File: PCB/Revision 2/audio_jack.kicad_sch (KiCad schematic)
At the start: 1 part, among them J3 AudioJack

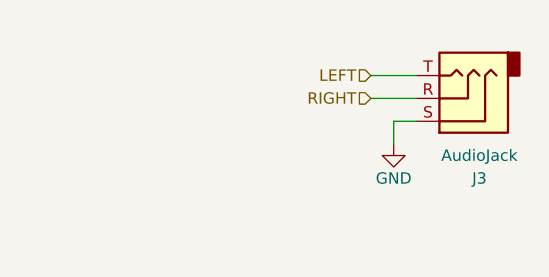
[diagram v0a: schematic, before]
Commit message: ESD protection diodes go BRRRRRRR
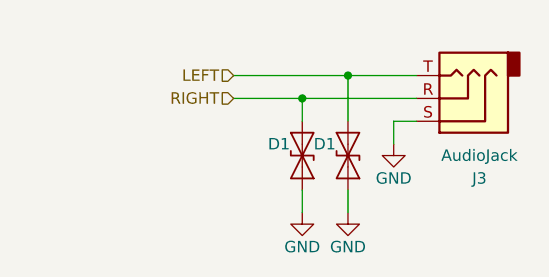
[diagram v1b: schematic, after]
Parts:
- added D1 (x2): ESD9B3.3ST5G, Diode_SMD:D_SOD-923, symbol Diode:ESD9B3.3ST5G
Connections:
- net GND: now also D1.2 (A2), D1.2 (A2)
- net LEFT: now also D1.1 (A1)
- net RIGHT: now also D1.1 (A1)
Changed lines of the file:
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@@
 (kicad_sch (version 20230121) (generator eeschema)
   (paper "USLetter")
+  (junction (at 130.81 86.36) (diameter 0) (color 0 0 0 0)
+  )
+  (junction (at 125.73 88.9) (diameter 0) (color 0 0 0 0)
+  )
+  (wire (pts (xy 130.81 86.36) (xy 138.43 86.36))
+    (stroke (width 0) (type default))
+  )
   (wire (pts (xy 135.89 91.44) (xy 138.43 91.44))
     (stroke (width 0) (type default))
   )
+  (wire (pts (xy 125.73 99.06) (xy 125.73 101.6))
+    (stroke (width 0) (type default))
+  )
   (wire (pts (xy 135.89 91.44) (xy 135.89 93.98))
     (stroke (width 0) (type default))
   )
-  (wire (pts (xy 133.35 88.9) (xy 138.43 88.9))
-    (stroke (width 0) (type default))
-  )
-  (wire (pts (xy 133.35 86.36) (xy 138.43 86.36))
-    (stroke (width 0) (type default))
-  )
-  (hierarchical_label "LEFT" (shape input) (at 133.35 86.36 180) (fields_autoplaced)
+  (wire (pts (xy 130.81 99.06) (xy 130.81 101.6))
+    (stroke (width 0) (type default))
+  )
+  (wire (pts (xy 118.11 88.9) (xy 125.73 88.9))
+    (stroke (width 0) (type default))
+  )
+  (wire (pts (xy 125.73 88.9) (xy 138.43 88.9))
+    (stroke (width 0) (type default))
+  )
+  (wire (pts (xy 118.11 86.36) (xy 130.81 86.36))
+    (stroke (width 0) (type default))
+  )
+  (wire (pts (xy 130.81 86.36) (xy 130.81 91.44))
+    (stroke (width 0) (type default))
+  )
+  (wire (pts (xy 125.73 88.9) (xy 125.73 91.44))
+    (stroke (width 0) (type default))
+  )
+  (hierarchical_label "LEFT" (shape input) (at 118.11 86.36 180) (fields_autoplaced)
     (effects (font (size 1.27 1.27)) (justify right))
   )
-  (hierarchical_label "RIGHT" (shape input) (at 133.35 88.9 180) (fields_autoplaced)
+  (hierarchical_label "RIGHT" (shape input) (at 118.11 88.9 180) (fields_autoplaced)
     (effects (font (size 1.27 1.27)) (justify right))
   )
@@
         (path "/3ba39048-ccb5-49b6-bc29-f9a8dd2e53b6/6aabb2d5-86ec-4e4f-b3fd-74d490a8ab06"
           (reference "#PWR0132") (unit 1)
+        )
+      )
+    )
+  )
+  (symbol (lib_id "Diode:ESD9B3.3ST5G") (at 125.73 95.25 270) (unit 1)
+    (in_bom yes) (on_board yes) (dnp no)
+    (property "Reference" "D1" (at 121.92 93.9799 90)
+      (effects (font (size 1.27 1.27)) (justify left))
+    )
+    (property "Value" "ESD9B3.3ST5G" (at 128.27 96.5199 90)
+      (effects (font (size 1.27 1.27)) (justify left) hide)
+    )
+    (property "Footprint" "Diode_SMD:D_SOD-923" (at 125.73 95.25 0)
+      (effects (font (size 1.27 1.27)) hide)
+    )
+    (property "Datasheet" "https://www.onsemi.com/pub/Collateral/ESD9B-D.PDF" (at 125.73 95.25 0)
+      (effects (font (size 1.27 1.27)) hide)
+    )
+    (pin "1")
+    (pin "2")
+    (instances
+      (project "Revision 2"
+        (path "/3ba39048-ccb5-49b6-bc29-f9a8dd2e53b6/e0049583-c97a-4b82-a4d7-59c894eac2f8"
+          (reference "D1") (unit 1)
+        )
+        (path "/3ba39048-ccb5-49b6-bc29-f9a8dd2e53b6/ef7f0437-b22e-4c24-9273-d90d53267996"
+          (reference "D1") (unit 1)
+        )
+        (path "/3ba39048-ccb5-49b6-bc29-f9a8dd2e53b6/05c17752-4e2f-4780-999c-64683914a9ff"
+          (reference "D18") (unit 1)
+        )
+        (path "/3ba39048-ccb5-49b6-bc29-f9a8dd2e53b6/c07b2ed0-3ddf-4a7b-83a6-b9bc424f9605"
+          (reference "D27") (unit 1)
+        )
+        (path "/3ba39048-ccb5-49b6-bc29-f9a8dd2e53b6/6aabb2d5-86ec-4e4f-b3fd-74d490a8ab06"
+          (reference "D41") (unit 1)
+        )
+      )
+    )
+  )
+  (symbol (lib_id "power:GND") (at 125.73 101.6 0) (unit 1)
+    (in_bom yes) (on_board yes) (dnp no)
+    (property "Reference" "#PWR031" (at 125.73 107.95 0)
+      (effects (font (size 1.27 1.27)) hide)
+    )
+    (property "Value" "GND" (at 125.73 105.41 0)
+      (effects (font (size 1.27 1.27)))
+    )
+    (property "Footprint" "" (at 125.73 101.6 0)
+      (effects (font (size 1.27 1.27)) hide)
+    )
+    (property "Datasheet" "" (at 125.73 101.6 0)
+      (effects (font (size 1.27 1.27)) hide)
+    )
+    (pin "1")
+    (instances
+      (project "Revision 2"
+        (path "/3ba39048-ccb5-49b6-bc29-f9a8dd2e53b6"
+          (reference "#PWR031") (unit 1)
+        )
+        (path "/3ba39048-ccb5-49b6-bc29-f9a8dd2e53b6/ef7f0437-b22e-4c24-9273-d90d53267996"
+          (reference "#PWR0154") (unit 1)
+        )
+        (path "/3ba39048-ccb5-49b6-bc29-f9a8dd2e53b6/05c17752-4e2f-4780-999c-64683914a9ff"
+          (reference "#PWR0168") (unit 1)
+        )
+        (path "/3ba39048-ccb5-49b6-bc29-f9a8dd2e53b6/c07b2ed0-3ddf-4a7b-83a6-b9bc424f9605"
+          (reference "#PWR0177") (unit 1)
+        )
+        (path "/3ba39048-ccb5-49b6-bc29-f9a8dd2e53b6/6aabb2d5-86ec-4e4f-b3fd-74d490a8ab06"
+          (reference "#PWR0191") (unit 1)
+        )
+      )
+    )
+  )
+  (symbol (lib_id "power:GND") (at 130.81 101.6 0) (unit 1)
+    (in_bom yes) (on_board yes) (dnp no)
+    (property "Reference" "#PWR031" (at 130.81 107.95 0)
+      (effects (font (size 1.27 1.27)) hide)
+    )
+    (property "Value" "GND" (at 130.81 105.41 0)
+      (effects (font (size 1.27 1.27)))
+    )
+    (property "Footprint" "" (at 130.81 101.6 0)
+      (effects (font (size 1.27 1.27)) hide)
+    )
+    (property "Datasheet" "" (at 130.81 101.6 0)
+      (effects (font (size 1.27 1.27)) hide)
+    )
+    (pin "1")
+    (instances
+      (project "Revision 2"
+        (path "/3ba39048-ccb5-49b6-bc29-f9a8dd2e53b6"
+          (reference "#PWR031") (unit 1)
+        )
+        (path "/3ba39048-ccb5-49b6-bc29-f9a8dd2e53b6/ef7f0437-b22e-4c24-9273-d90d53267996"
+          (reference "#PWR0154") (unit 1)
+        )
+        (path "/3ba39048-ccb5-49b6-bc29-f9a8dd2e53b6/05c17752-4e2f-4780-999c-64683914a9ff"
+          (reference "#PWR0168") (unit 1)
+        )
+        (path "/3ba39048-ccb5-49b6-bc29-f9a8dd2e53b6/c07b2ed0-3ddf-4a7b-83a6-b9bc424f9605"
+          (reference "#PWR0177") (unit 1)
+        )
+        (path "/3ba39048-ccb5-49b6-bc29-f9a8dd2e53b6/6aabb2d5-86ec-4e4f-b3fd-74d490a8ab06"
+          (reference "#PWR0190") (unit 1)
         )
       )
@@
         )
       )
+    )
+  )
+  (symbol (lib_id "Diode:ESD9B3.3ST5G") (at 130.81 95.25 270) (unit 1)
+    (in_bom yes) (on_board yes) (dnp no)
+    (property "Reference" "D1" (at 127 93.9799 90)
+      (effects (font (size 1.27 1.27)) (justify left))
+    )
+    (property "Value" "ESD9B3.3ST5G" (at 133.35 96.5199 90)
+      (effects (font (size 1.27 1.27)) (justify left) hide)
+    )
+    (property "Footprint" "Diode_SMD:D_SOD-923" (at 130.81 95.25 0)
+      (effects (font (size 1.27 1.27)) hide)
+    )
+    (property "Datasheet" "https://www.onsemi.com/pub/Collateral/ESD9B-D.PDF" (at 130.81 95.25 0)
+      (effects (font (size 1.27 1.27)) hide)
+    )
+    (pin "1")
+    (pin "2")
+    (instances
+      (project "Revision 2"
+        (path "/3ba39048-ccb5-49b6-bc29-f9a8dd2e53b6/e0049583-c97a-4b82-a4d7-59c894eac2f8"
+          (reference "D1") (unit 1)
+        )
+        (path "/3ba39048-ccb5-49b6-bc29-f9a8dd2e53b6/ef7f0437-b22e-4c24-9273-d90d53267996"
+          (reference "D1") (unit 1)
+        )
+        (path "/3ba39048-ccb5-49b6-bc29-f9a8dd2e53b6/05c17752-4e2f-4780-999c-64683914a9ff"
+          (reference "D18") (unit 1)
+        )
+        (path "/3ba39048-ccb5-49b6-bc29-f9a8dd2e53b6/c07b2ed0-3ddf-4a7b-83a6-b9bc424f9605"
+          (reference "D27") (unit 1)
+        )
+        (path "/3ba39048-ccb5-49b6-bc29-f9a8dd2e53b6/6aabb2d5-86ec-4e4f-b3fd-74d490a8ab06"
+          (reference "D40") (unit 1)
+        )
+      )

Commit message: Updated re: issue #2
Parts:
- added FB1, FB2: FerriteBead_Small, symbol Device:FerriteBead_Small
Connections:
- net LEFT: now also FB1.2; no longer D1.1 (A1), J3.T
- net RIGHT: now also FB2.2; no longer D1.1 (A1), J3.R
- new net: D1.1 (A1), FB2.1, J3.R
- new net: D1.1 (A1), FB1.1, J3.T
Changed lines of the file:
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@@
+    (stroke (width 0) (type default))
+  )
+  (wire (pts (xy 118.11 88.9) (xy 125.73 88.9))
+    (stroke (width 0) (type default))
+  )
+  (wire (pts (xy 102.87 86.36) (xy 111.76 86.36))
     (stroke (width 0) (type default))
   )
@@
     (stroke (width 0) (type default))
   )
-  (wire (pts (xy 118.11 88.9) (xy 125.73 88.9))
+  (wire (pts (xy 116.84 86.36) (xy 130.81 86.36))
     (stroke (width 0) (type default))
   )
@@
     (stroke (width 0) (type default))
   )
-  (wire (pts (xy 118.11 86.36) (xy 130.81 86.36))
-    (stroke (width 0) (type default))
-  )
   (wire (pts (xy 130.81 86.36) (xy 130.81 91.44))
     (stroke (width 0) (type default))
   )
+  (wire (pts (xy 102.87 88.9) (xy 113.03 88.9))
+    (stroke (width 0) (type default))
+  )
   (wire (pts (xy 125.73 88.9) (xy 125.73 91.44))
     (stroke (width 0) (type default))
   )
-  (hierarchical_label "LEFT" (shape input) (at 118.11 86.36 180) (fields_autoplaced)
+  (hierarchical_label "LEFT" (shape input) (at 102.87 86.36 180) (fields_autoplaced)
     (effects (font (size 1.27 1.27)) (justify right))
   )
-  (hierarchical_label "RIGHT" (shape input) (at 118.11 88.9 180) (fields_autoplaced)
+  (hierarchical_label "RIGHT" (shape input) (at 102.87 88.9 180) (fields_autoplaced)
     (effects (font (size 1.27 1.27)) (justify right))
   )
@@
         (path "/3ba39048-ccb5-49b6-bc29-f9a8dd2e53b6/6aabb2d5-86ec-4e4f-b3fd-74d490a8ab06"
           (reference "D41") (unit 1)
+        )
+      )
+    )
+  )
+  (symbol (lib_id "Device:FerriteBead_Small") (at 115.57 88.9 270) (unit 1)
+    (in_bom yes) (on_board yes) (dnp no)
+    (property "Reference" "FB2" (at 118.1481 91.44 90)
+      (effects (font (size 1.27 1.27)))
+    )
+    (property "Value" "FerriteBead_Small" (at 111.7981 93.98 90)
+      (effects (font (size 1.27 1.27)))
+    )
+    (property "Footprint" "" (at 115.57 87.122 90)
+      (effects (font (size 1.27 1.27)) hide)
+    )
+    (property "Datasheet" "~" (at 115.57 88.9 0)
+      (effects (font (size 1.27 1.27)) hide)
+    )
+    (pin "1")
+    (pin "2")
+    (instances
+      (project "Revision 2"
+        (path "/3ba39048-ccb5-49b6-bc29-f9a8dd2e53b6/6aabb2d5-86ec-4e4f-b3fd-74d490a8ab06"
+          (reference "FB2") (unit 1)
         )
       )
@@
         )
       )
+    )
+  )
+  (symbol (lib_id "Device:FerriteBead_Small") (at 114.3 86.36 270) (unit 1)
+    (in_bom yes) (on_board yes) (dnp no)
+    (property "Reference" "FB1" (at 118.1481 83.82 90)
+      (effects (font (size 1.27 1.27)))
+    )
+    (property "Value" "FerriteBead_Small" (at 114.3381 81.28 90)
+      (effects (font (size 1.27 1.27)))
+    )
+    (property "Footprint" "" (at 114.3 84.582 90)
+      (effects (font (size 1.27 1.27)) hide)
+    )
+    (property "Datasheet" "~" (at 114.3 86.36 0)
+      (effects (font (size 1.27 1.27)) hide)
+    )
+    (pin "1")
+    (pin "2")
+    (instances
+      (project "Revision 2"
+        (path "/3ba39048-ccb5-49b6-bc29-f9a8dd2e53b6/6aabb2d5-86ec-4e4f-b3fd-74d490a8ab06"
+          (reference "FB1") (unit 1)
+        )
+      )
